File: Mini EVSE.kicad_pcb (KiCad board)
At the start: 2 copper layers, 49.5 x 76.8 mm, 49 parts, among them IC1 ATtiny84-20P, IC2 UCC23511QDWYRQ1, IC3 TLP3547_TP1,F_O, IC4 ISO224ADWV, J1 ICP, SW1 SW_DIP_x01, X1 15.36MHz

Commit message: Final touch
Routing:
- net /RE+: track 37.0 -> 38.3 mm, vias 1 -> 2
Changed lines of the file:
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@@
   (segment (start 142.92 104.5) (end 145.46 104.5) (width 1.016) (layer "F.Cu") (net 11))
   (segment (start 142.92 104.5) (end 142.92 105.28) (width 1.016) (layer "F.Cu") (net 11))
+  (segment (start 141.85 106.35) (end 140.6 106.35) (width 1.016) (layer "F.Cu") (net 11))
   (via (at 141.85 106.35) (size 0.6) (drill 0.4) (layers "F.Cu" "B.Cu") (net 11))
+  (via (at 140.6 106.35) (size 0.6) (drill 0.4) (layers "F.Cu" "B.Cu") (net 11))
   (segment (start 114.98177 108.42823) (end 117.06 106.35) (width 1.016) (layer "B.Cu") (net 11))
+  (segment (start 117.06 106.35) (end 140.6 106.35) (width 1.016) (layer "B.Cu") (net 11))
   (segment (start 110.5 108.42823) (end 114.98177 108.42823) (width 1.016) (layer "B.Cu") (net 11))
-  (segment (start 117.06 106.35) (end 141.85 106.35) (width 1.016) (layer "B.Cu") (net 11))
+  (segment (start 140.6 106.35) (end 141.85 106.35) (width 1.016) (layer "B.Cu") (net 11))
   (segment (start 107.25 91.875) (end 107.1875 91.9375) (width 1.016) (layer "F.Cu") (net 12))
   (segment (start 119.6 114.6) (end 121.117 113.083) (width 1.016) (layer "F.Cu") (net 12))

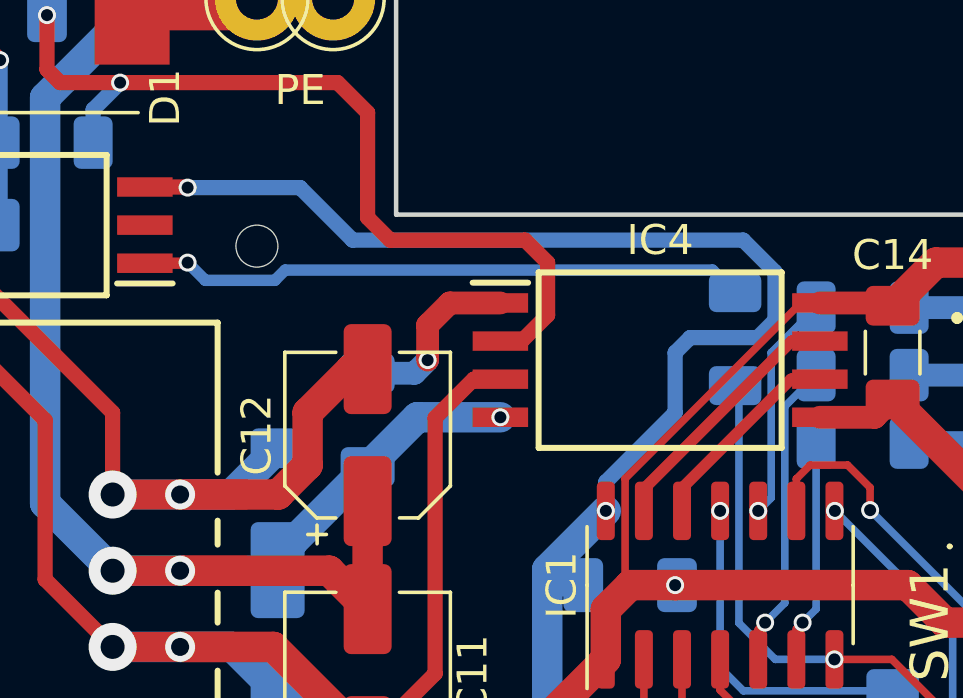
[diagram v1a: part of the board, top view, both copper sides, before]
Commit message: A bit more safety distance
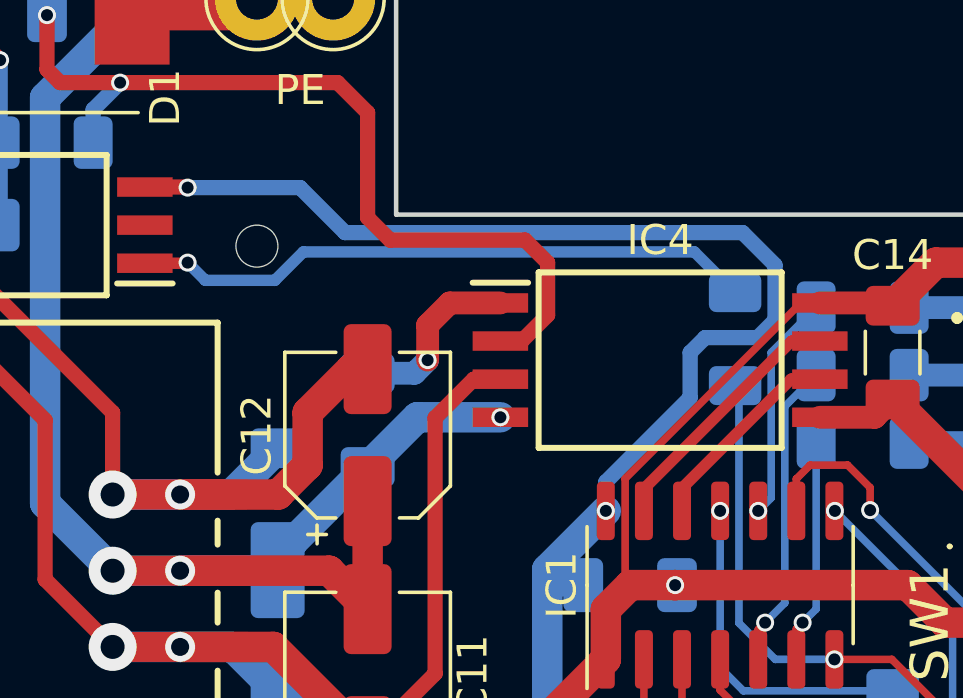
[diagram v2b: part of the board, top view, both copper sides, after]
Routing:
- net Net-(IC2-Pad1): track 20.4 -> 20.9 mm
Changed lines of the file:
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@@
   (segment (start 145.555 87.75) (end 147.805 90) (width 1.016) (layer "B.Cu") (net 2))
   (segment (start 140.5 90) (end 140.5 93.431) (width 1.016) (layer "B.Cu") (net 2))
+  (segment (start 133.25 70) (end 120 70) (width 0.508) (layer "B.Cu") (net 2))
   (segment (start 145.555 87.75) (end 146.482 86.823) (width 1.016) (layer "B.Cu") (net 2))
   (segment (start 129.42 93) (end 129.42 90.08) (width 1.016) (layer "B.Cu") (net 2))
   (segment (start 140.5 90) (end 140.5 89.25) (width 1.016) (layer "B.Cu") (net 2))
-  (segment (start 134.329 71.308394) (end 134.329 72.921) (width 0.508) (layer "B.Cu") (net 2))
-  (segment (start 118.5 68.5) (end 120.25 70.25) (width 0.508) (layer "B.Cu") (net 2))
+  (segment (start 134.329 72.921) (end 134.329 71.079) (width 0.508) (layer "B.Cu") (net 2))
   (segment (start 135.3625 86.5) (end 135.3625 89.8625) (width 1.016) (layer "B.Cu") (net 2))
-  (segment (start 134.329 72.921) (end 133.75 73.5) (width 0.508) (layer "B.Cu") (net 2))
   (segment (start 126.7375 88.9875) (end 127.75 90) (width 1.016) (layer "B.Cu") (net 2))
   (segment (start 135.5 90) (end 140.5 90) (width 1.016) (layer "B.Cu") (net 2))
   (segment (start 142 87.75) (end 145.555 87.75) (width 1.016) (layer "B.Cu") (net 2))
+  (segment (start 118.5 68.5) (end 114.75 68.5) (width 0.508) (layer "B.Cu") (net 2))
   (segment (start 127.9375 81.75) (end 126.75 81.75) (width 0.762) (layer "B.Cu") (net 2))
   (segment (start 126.7375 81.2275) (end 128.69 79.275) (width 1.016) (layer "B.Cu") (net 2))
-  (segment (start 133.270606 70.25) (end 134.329 71.308394) (width 0.508) (layer "B.Cu") (net 2))
+  (segment (start 131.5 74) (end 132 73.5) (width 0.508) (layer "B.Cu") (net 2))
   (segment (start 126.7375 81.7625) (end 126.7375 81.2275) (width 1.016) (layer "B.Cu") (net 2))
   (segment (start 129.5 90) (end 135.5 90) (width 1.016) (layer "B.Cu") (net 2))
   (segment (start 146.482 80.46) (end 146.482 85.54) (width 1.27) (layer "B.Cu") (net 2))
   (segment (start 146.482 86.823) (end 146.482 85.54) (width 1.016) (layer "B.Cu") (net 2))
-  (segment (start 131 74) (end 131 76) (width 0.508) (layer "B.Cu") (net 2))
   (segment (start 140.5 93.431) (end 142.569 95.5) (width 1.016) (layer "B.Cu") (net 2))
+  (segment (start 131.5 75.5) (end 131.5 74) (width 0.508) (layer "B.Cu") (net 2))
   (segment (start 135.3625 89.8625) (end 135.5 90) (width 0.25) (layer "B.Cu") (net 2))
-  (segment (start 120.25 70.25) (end 133.270606 70.25) (width 0.508) (layer "B.Cu") (net 2))
   (segment (start 141.402 80.46) (end 146.482 80.46) (width 1.27) (layer "B.Cu") (net 2))
+  (segment (start 132 73.5) (end 133.75 73.5) (width 0.508) (layer "B.Cu") (net 2))
   (segment (start 142.569 95.5) (end 142.92 95.5) (width 1.016) (layer "B.Cu") (net 2))
-  (segment (start 133.75 73.5) (end 131.5 73.5) (width 0.508) (layer "B.Cu") (net 2))
   (segment (start 129.42 90.08) (end 129.5 90) (width 1.016) (layer "B.Cu") (net 2))
-  (segment (start 114.75 68.5) (end 118.5 68.5) (width 0.508) (layer "B.Cu") (net 2))
-  (segment (start 131.5 73.5) (end 131 74) (width 0.508) (layer "B.Cu") (net 2))
+  (segment (start 128.69 79.275) (end 128.69 78.31) (width 0.508) (layer "B.Cu") (net 2))
   (segment (start 129.42 95.25) (end 129.42 93) (width 1.016) (layer "B.Cu") (net 2))
-  (segment (start 131 76) (end 128.69 78.31) (width 0.508) (layer "B.Cu") (net 2))
   (segment (start 126.75 81.75) (end 126.7375 81.7625) (width 0.762) (layer "B.Cu") (net 2))
+  (segment (start 133.75 73.5) (end 134.329 72.921) (width 0.508) (layer "B.Cu") (net 2))
   (segment (start 129.42 96.045) (end 130.375 97) (width 1.016) (layer "B.Cu") (net 2))
   (segment (start 140.5 89.25) (end 142 87.75) (width 1.016) (layer "B.Cu") (net 2))
   (segment (start 126.7375 86.5) (end 126.7375 81.7625) (width 1.016) (layer "B.Cu") (net 2))
+  (segment (start 128.69 78.31) (end 131.5 75.5) (width 0.508) (layer "B.Cu") (net 2))
   (segment (start 126.7375 88.9875) (end 126.7375 86.5) (width 1.016) (layer "B.Cu") (net 2))
-  (segment (start 128.69 78.31) (end 128.69 79.275) (width 0.508) (layer "B.Cu") (net 2))
+  (segment (start 134.329 71.079) (end 133.25 70) (width 0.508) (layer "B.Cu") (net 2))
   (segment (start 127.75 90) (end 129.5 90) (width 1.016) (layer "B.Cu") (net 2))
+  (segment (start 120 70) (end 118.5 68.5) (width 0.508) (layer "B.Cu") (net 2))
   (segment (start 135.191 72.345) (end 135.825 72.345) (width 0.254) (layer "F.Cu") (net 3))
   (segment (start 129.5 81.75) (end 128.69 82.56) (width 1.016) (layer "F.Cu") (net 3))
@@
   (segment (start 114.73 71.02) (end 114.75 71) (width 0.254) (layer "F.Cu") (net 21))
   (via (at 114.75 71) (size 0.6) (drill 0.4) (layers "F.Cu" "B.Cu") (net 21))
-  (segment (start 133 72) (end 132.25 71.25) (width 0.381) (layer "B.Cu") (net 21))
-  (segment (start 118 71.25) (end 117.659499 71.590501) (width 0.381) (layer "B.Cu") (net 21))
-  (segment (start 117.659499 71.590501) (end 115.340501 71.590501) (width 0.381) (layer "B.Cu") (net 21))
-  (segment (start 115.340501 71.590501) (end 114.75 71) (width 0.381) (layer "B.Cu") (net 21))
-  (segment (start 132.25 71.25) (end 118 71.25) (width 0.381) (layer "B.Cu") (net 21))
+  (segment (start 131.6445 70.6445) (end 133 72) (width 0.381) (layer "B.Cu") (net 21))
+  (segment (start 114.75 71) (end 115.340501 71.590501) (width 0.381) (layer "B.Cu") (net 21))
+  (segment (start 118.6055 70.6445) (end 131.6445 70.6445) (width 0.381) (layer "B.Cu") (net 21))
+  (segment (start 117.659499 71.590501) (end 118.6055 70.6445) (width 0.381) (layer "B.Cu") (net 21))
+  (segment (start 115.340501 71.590501) (end 117.659499 71.590501) (width 0.381) (layer "B.Cu") (net 21))
   (segment (start 102.675 69.75) (end 104 69.75) (width 0.508) (layer "F.Cu") (net 23))
   (via (at 104 69.75) (size 0.6) (drill 0.4) (layers "F.Cu" "B.Cu") (net 23))
